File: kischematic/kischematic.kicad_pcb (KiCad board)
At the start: 2 copper layers, 26.7 x 50 mm, 109 parts, among them IC1 BlueNRG, IC10 128x64OLED, IC2 EFM32ZG108, IC3 BQ297xx, IC4 AAT3672IWO-4.2-1, IC5 TPS6223xx, IC6 APDS-9303, IC7 APDS-9303, IC8 BSD840NH6327XTSA1, IC9 MMA8653FC, J1 Screw_Terminal_1x02, J2 Screw_Terminal_1x01, J3 Screw_Terminal_1x01, J4 0, J5 Screw_Terminal_1x01, J6 Screw_Terminal_1x01, P1 CONN_01X01, P2 CONN_01X01, P3 CONN_01X01, P4 CONN_01X01, P5 CONN_01X01, P6 CONN_01X01, P7 CONN_01X01, P8 CONN_01X04, P9 CONN_01X04, SW1 SW_Push, SW2 SW_Push, U1 USB-C, U2 SWD_SPRING, Y1 32k, Y2 16M

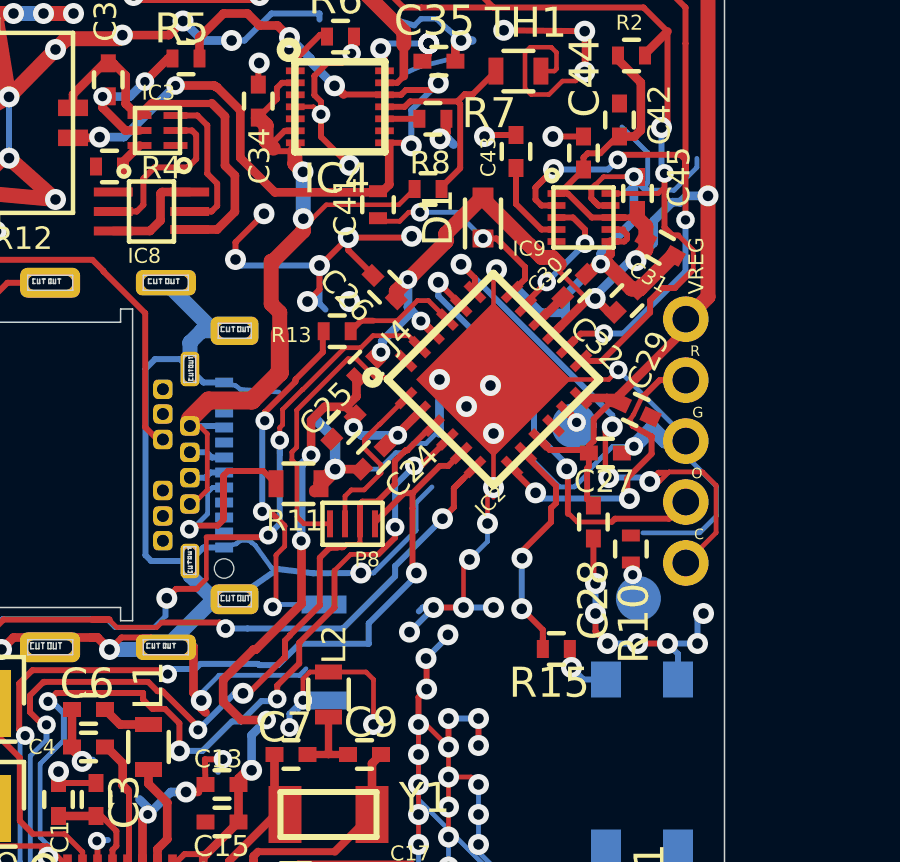
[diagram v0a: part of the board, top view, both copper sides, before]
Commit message: Routing problem caused by diode change; fix missing edge cuts.
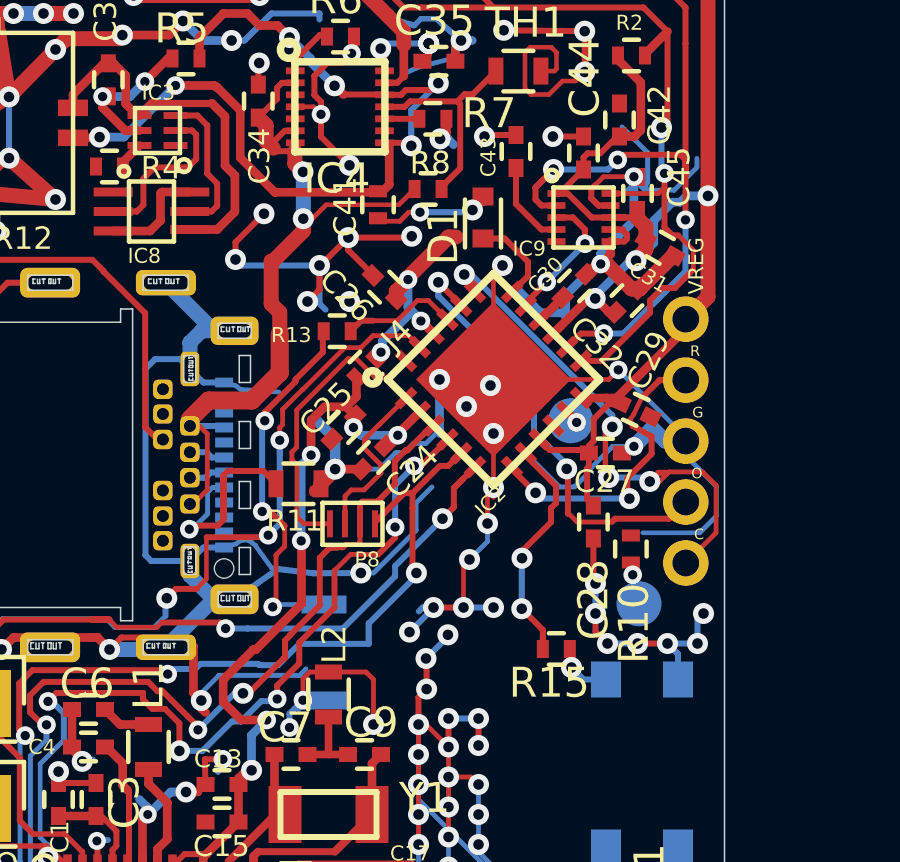
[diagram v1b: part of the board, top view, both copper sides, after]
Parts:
- C1, C2: value 100p -> HP100p
- C10, C8: value 15p -> HP15p
- C11, C13, C16, C4: value 1u -> HP1u
- C12, C14, C15, C5, C6: value 100n -> HP100n
- C17, C22: value 56p -> HP56p
- C18, C21, C23: value p5 -> HPp5
- C19, C20: value 1p3 -> HP1p3
- C3: value 150n -> HP150n
- C7, C9: value 22p -> HP22p
- D1: value D -> 0.8V FVD
- L1: value 10u -> DC-DC 4u7
- L4, L6: value 1n3 -> MQ 1n3
- L5: value 2n4 -> MQ 2n4
- L7: value 5n6 -> MQ 5n6
- L8: value 1u -> DC-DC 1u
- moved PIEZO 0.20 mm to (97.6, 47.4)
- moved PIEZOG 0.18 mm to (99.8, 53.5)
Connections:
- D1 pad 1: Net-(C41-Pad1) -> Net-(D1-Pad1)
- D1 pad 2: VREG -> Net-(C41-Pad1)
- IC2 pad 18: Net-(C41-Pad1) -> Net-(D1-Pad1)
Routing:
- net VREG: track 200.6 -> 193.8 mm
- net Net-(D1-Pad1): track 0.00 -> 3.05 mm
- net Net-(C41-Pad1): track 6.79 -> 4.03 mm
- net SWCLK: track 18.2 -> 17.5 mm
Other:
- outline, holes or cut-outs redrawn

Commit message: Mess.
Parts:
- removed PIEZO, PIEZOG: TEST, newlightmeter:SMALLWIREPAD
- added J7: 0, Resistors_SMD:R_0402, F.Cu at (95.5, 41.4)
- added TP1: TEST, newlightmeter:SMALLWIREPAD, B.Cu at (97.6, 47.4)
- added TP2: TEST, newlightmeter:SMALLWIREPAD, B.Cu at (99.9, 53.5)
- added U3: USB_PROTECTION, Housings_DFN_QFN:DFN-6-1EP_2x2mm_Pitch0.5mm, F.Cu at (81.2, 46.6)
- moved D1 1.00 mm to (94.7, 39.6)
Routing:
- net VREG: track 193.8 -> 198.4 mm, vias 21 -> 22
- net GND: track 476.7 -> 472.4 mm
- net (no net): track 2.40 -> 5.41 mm
- net Net-(C41-Pad1): track 4.03 -> 4.46 mm, vias 2 -> 0
- net ACCELINT1: track 4.48 -> 4.52 mm, vias 2 -> 0

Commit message: More work on USB stuff.
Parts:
- U3: value USB_PROTECTION -> FT220X; footprint Housings_DFN_QFN:DFN-6-1EP_2x2mm_Pitch0.5mm -> newlightmeter:QFN_16
- moved U3 11.0 mm to (71.7, 52.1)
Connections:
- U1 pad B6: Net-(U1-PadA7) -> Net-(U1-PadA6)
- U1 pad B7: Net-(U1-PadA6) -> Net-(U1-PadA7)
- U3 pad 1: Net-(U1-PadA6) -> Net-(U3-Pad1)
- U3 pad 2: Net-(U1-PadA7) -> Net-(U3-Pad2)
- U3 pad 4: (no net) -> Net-(U3-Pad4)
- U3 pad 5: (no net) -> Net-(U3-Pad5)
- U3 pad 6: VUSB -> Net-(U3-Pad6)
- U3 pad 7: GND -> Net-(U3-Pad7)
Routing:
- net Net-(U1-PadA7): track 1.27 -> 0.05 mm
- net Net-(U1-PadA6): track 1.26 -> 0.06 mm
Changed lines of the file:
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@@
 (kicad_pcb (version 20160815) (host pcbnew "(2016-12-18 revision 3ffa37c)-master")
   (general
-    (links 266)
-    (no_connects 13)
+    (links 261)
+    (no_connects 10)
     (area 75.974999 24.974999 102.725001 75.025001)
     (thickness 1.6)
     (drawings 272)
-    (tracks 2039)
+    (tracks 2033)
     (zones 0)
     (modules 111)
-    (nets 109)
+    (nets 125)
   )
   (page A4)
@@
   (net 107 "Net-(D1-Pad1)")
   (net 108 "Net-(U3-Pad3)")
+  (net 109 "Net-(U3-Pad7)")
+  (net 110 "Net-(U3-Pad6)")
+  (net 111 "Net-(U3-Pad5)")
+  (net 112 "Net-(U3-Pad4)")
+  (net 113 "Net-(U3-Pad2)")
+  (net 114 "Net-(U3-Pad1)")
+  (net 115 "Net-(U3-Pad8)")
+  (net 116 "Net-(U3-Pad9)")
+  (net 117 "Net-(U3-Pad10)")
+  (net 118 "Net-(U3-Pad11)")
+  (net 119 "Net-(U3-Pad12)")
+  (net 120 "Net-(U3-Pad13)")
+  (net 121 "Net-(U3-Pad14)")
+  (net 122 "Net-(U3-Pad15)")
+  (net 123 "Net-(U3-Pad16)")
+  (net 124 "Net-(U3-Pad17)")
   (net_class Default "This is the default net class."
     (clearance 0.1525)
@@
     (add_net "Net-(U1-PadB3)")
     (add_net "Net-(U1-PadB8)")
+    (add_net "Net-(U3-Pad1)")
+    (add_net "Net-(U3-Pad10)")
+    (add_net "Net-(U3-Pad11)")
+    (add_net "Net-(U3-Pad12)")
+    (add_net "Net-(U3-Pad13)")
+    (add_net "Net-(U3-Pad14)")
+    (add_net "Net-(U3-Pad15)")
+    (add_net "Net-(U3-Pad16)")
+    (add_net "Net-(U3-Pad17)")
+    (add_net "Net-(U3-Pad2)")
     (add_net "Net-(U3-Pad3)")
+    (add_net "Net-(U3-Pad4)")
+    (add_net "Net-(U3-Pad5)")
+    (add_net "Net-(U3-Pad6)")
+    (add_net "Net-(U3-Pad7)")
+    (add_net "Net-(U3-Pad8)")
+    (add_net "Net-(U3-Pad9)")
     (add_net PIEZO)
     (add_net PIEZOGND)
@@
     (add_net VUSB)
   )
-  (module Housings_DFN_QFN:DFN-6-1EP_2x2mm_Pitch0.5mm (layer F.Cu)
-    (at 81.2 46.62)
-    (descr "DC6 Package; 6-Lead Plastic DFN (2mm x 2mm) (see Linear Technology DFN_6_05-08-1703.pdf)")
-    (tags "DFN 0.5")
-    (attr smd)
-    (fp_text reference U3 (at 0 -2.05) (layer F.SilkS)
-      (effects (font (size 1 1) (thickness 0.15)))
-    )
-    (fp_text value USB_PROTECTION (at 0 2.05) (layer F.Fab)
-      (effects (font (size 1 1) (thickness 0.15)))
-    )
-    (fp_line (start -1.35 -1.125) (end 0.575 -1.125) (layer F.SilkS) (width 0.15))
-    (fp_line (start -0.575 1.125) (end 0.575 1.125) (layer F.SilkS) (width 0.15))
-    (fp_line (start -1.55 1.3) (end 1.55 1.3) (layer F.CrtYd) (width 0.05))
-    (fp_line (start -1.55 -1.3) (end 1.55 -1.3) (layer F.CrtYd) (width 0.05))
-    (fp_line (start 1.55 -1.3) (end 1.55 1.3) (layer F.CrtYd) (width 0.05))
-    (fp_line (start -1.55 -1.3) (end -1.55 1.3) (layer F.CrtYd) (width 0.05))
-    (fp_line (start -1 0) (end 0 -1) (layer F.Fab) (width 0.15))
-    (fp_line (start -1 1) (end -1 0) (layer F.Fab) (width 0.15))
-    (fp_line (start 1 1) (end -1 1) (layer F.Fab) (width 0.15))
-    (fp_line (start 1 -1) (end 1 1) (layer F.Fab) (width 0.15))
-    (fp_line (start 0 -1) (end 1 -1) (layer F.Fab) (width 0.15))
-    (pad 7 smd rect (at 0 -0.355) (size 0.61 0.71) (layers F.Cu F.Paste F.Mask)
-      (net 1 GND) (solder_paste_margin_ratio -0.2))
-    (pad 7 smd rect (at 0 0.355) (size 0.61 0.71) (layers F.Cu F.Paste F.Mask)
-      (net 1 GND) (solder_paste_margin_ratio -0.2))
-    (pad 6 smd rect (at 0.925 -0.5) (size 0.7 0.25) (layers F.Cu F.Paste F.Mask)
-      (net 43 VUSB))
-    (pad 5 smd rect (at 0.925 0) (size 0.7 0.25) (layers F.Cu F.Paste F.Mask))
-    (pad 4 smd rect (at 0.925 0.5) (size 0.7 0.25) (layers F.Cu F.Paste F.Mask))
-    (pad 3 smd rect (at -0.925 0.5) (size 0.7 0.25) (layers F.Cu F.Paste F.Mask)
-      (net 108 "Net-(U3-Pad3)"))
-    (pad 2 smd rect (at -0.925 0) (size 0.7 0.25) (layers F.Cu F.Paste F.Mask)
-      (net 57 "Net-(U1-PadA7)"))
-    (pad 1 smd rect (at -0.925 -0.5) (size 0.7 0.25) (layers F.Cu F.Paste F.Mask)
-      (net 56 "Net-(U1-PadA6)"))
-    (model Housings_DFN_QFN.3dshapes/DFN-6-1EP_2x2mm_Pitch0.5mm.wrl
-      (at (xyz 0 0 0))
-      (scale (xyz 1 1 1))
-      (rotate (xyz 0 0 0))
+  (module newlightmeter:QFN_16 (layer F.Cu)
+    (at 71.7 52.125)
+    (attr smd)
+    (fp_text reference U3 (at 0 -3.55) (layer F.SilkS)
+      (effects (font (size 1 1) (thickness 0.15)))
+    )
+    (fp_text value FT220X (at 0 3.55) (layer F.Fab)
+      (effects (font (size 1 1) (thickness 0.15)))
     )
+    (fp_line (start -2 -1.625) (end -1.625 -2) (layer F.SilkS) (width 0.15))
+    (fp_line (start 1.625 -2) (end 2 -2) (layer F.SilkS) (width 0.15))
+    (fp_line (start 2 -2) (end 2 -1.625) (layer F.SilkS) (width 0.15))
+    (fp_line (start -1.625 2) (end -2 2) (layer F.SilkS) (width 0.15))
+    (fp_line (start -2 2) (end -2 1.625) (layer F.SilkS) (width 0.15))
+    (fp_line (start 1.625 2) (end 2 2) (layer F.SilkS) (width 0.15))
+    (fp_line (start 2 2) (end 2 1.625) (layer F.SilkS) (width 0.15))
+    (fp_line (start -2.3 -2.3) (end 2.3 -2.3) (layer F.CrtYd) (width 0.05))
+    (fp_line (start 2.3 -2.3) (end 2.3 2.3) (layer F.CrtYd) (width 0.05))
+    (fp_line (start 2.3 2.3) (end -2.3 2.3) (layer F.CrtYd) (width 0.05))
+    (fp_line (start -2.3 2.3) (end -2.3 -2.3) (layer F.CrtYd) (width 0.05))
+    (pad 1 smd rect (at -2 -0.975 90) (size 0.4 1.1) (layers F.Cu F.Paste F.Mask)
+      (net 114 "Net-(U3-Pad1)"))
+    (pad 2 smd rect (at -2 -0.325 90) (size 0.4 1.1) (layers F.Cu F.Paste F.Mask)
+      (net 113 "Net-(U3-Pad2)"))
+    (pad 3 smd rect (at -2 0.325 90) (size 0.4 1.1) (layers F.Cu F.Paste F.Mask)
+      (net 108 "Net-(U3-Pad3)"))
+    (pad 4 smd rect (at -2 0.975 90) (size 0.4 1.1) (layers F.Cu F.Paste F.Mask)
+      (net 112 "Net-(U3-Pad4)"))
+    (pad 5 smd rect (at -0.975 2) (size 0.4 1.1) (layers F.Cu F.Paste F.Mask)
+      (net 111 "Net-(U3-Pad5)"))
+    (pad 6 smd rect (at -0.325 2) (size 0.4 1.1) (layers F.Cu F.Paste F.Mask)
+      (net 110 "Net-(U3-Pad6)"))
+    (pad 7 smd rect (at 0.325 2) (size 0.4 1.1) (layers F.Cu F.Paste F.Mask)
+      (net 109 "Net-(U3-Pad7)"))
+    (pad 8 smd rect (at 0.975 2) (size 0.4 1.1) (layers F.Cu F.Paste F.Mask)
+      (net 115 "Net-(U3-Pad8)"))
+    (pad 9 smd rect (at 2 0.975 90) (size 0.4 1.1) (layers F.Cu F.Paste F.Mask)
+      (net 116 "Net-(U3-Pad9)"))
+    (pad 10 smd rect (at 2 0.325 90) (size 0.4 1.1) (layers F.Cu F.Paste F.Mask)
+      (net 117 "Net-(U3-Pad10)"))
+    (pad 11 smd rect (at 2 -0.325 90) (size 0.4 1.1) (layers F.Cu F.Paste F.Mask)
+      (net 118 "Net-(U3-Pad11)"))
+    (pad 12 smd rect (at 2 -0.975 90) (size 0.4 1.1) (layers F.Cu F.Paste F.Mask)
+      (net 119 "Net-(U3-Pad12)"))
+    (pad 13 smd rect (at 0.975 -2) (size 0.4 1.1) (layers F.Cu F.Paste F.Mask)
+      (net 120 "Net-(U3-Pad13)"))
+    (pad 14 smd rect (at 0.325 -2) (size 0.4 1.1) (layers F.Cu F.Paste F.Mask)
+      (net 121 "Net-(U3-Pad14)"))
+    (pad 15 smd rect (at -0.325 -2) (size 0.4 1.1) (layers F.Cu F.Paste F.Mask)
+      (net 122 "Net-(U3-Pad15)"))
+    (pad 16 smd rect (at -0.975 -2) (size 0.4 1.1) (layers F.Cu F.Paste F.Mask)
+      (net 123 "Net-(U3-Pad16)"))
+    (pad 17 smd rect (at 0 -0.075) (size 2.15 2.15) (layers F.Cu F.Paste F.Mask)
+      (net 124 "Net-(U3-Pad17)"))
   )
   (module newlightmeter:AN2051 (layer F.Cu)
@@
       (net 43 VUSB))
     (pad B6 thru_hole roundrect (at 0.425 -1.14 90) (size 0.65 0.65) (drill 0.4) (layers *.Cu *.Mask)(roundrect_rratio 0.25)
-      (net 57 "Net-(U1-PadA7)"))
+      (net 56 "Net-(U1-PadA6)"))
     (pad B11 thru_hole roundrect (at -2.525 -2.04 90) (size 0.65 0.65) (drill 0.4) (layers *.Cu *.Mask)(roundrect_rratio 0.25)
       (net 65 "Net-(U1-PadB11)"))
@@
       (net 66 "Net-(R12-Pad2)"))
     (pad B7 thru_hole roundrect (at -0.425 -1.14 90) (size 0.65 0.65) (drill 0.4) (layers *.Cu *.Mask)(roundrect_rratio 0.25)
-      (net 56 "Net-(U1-PadA6)"))
+      (net 57 "Net-(U1-PadA7)"))
     (pad S4 thru_hole roundrect (at 6.075 -5.8 90) (size 1 2) (drill oval 0.5 1.5) (layers *.Cu *.Mask)(roundrect_rratio 0.25)
       (net 1 GND))
@@
   (segment (start 101.24 28.9) (end 100.73 29.41) (width 0.16) (layer F.Cu) (net 53) (status 10))
   (segment (start 101.31 28.9) (end 101.24 28.9) (width 0.16) (layer F.Cu) (net 53) (status 30))
-  (segment (start 85.395 49.275) (end 85.57 49.1) (width 0.2) (layer B.Cu) (net 56))
-  (segment (start 85.57 49.1) (end 86.02 49.1) (width 0.2) (layer B.Cu) (net 56) (status 20))
-  (segment (start 84.88 49.275) (end 85.395 49.275) (width 0.2) (layer B.Cu) (net 56) (status 10))
-  (segment (start 84.88 49.275) (end 84.835 49.275) (width 0.16) (layer B.Cu) (net 56) (status 30))
-  (segment (start 85.435 48.425) (end 85.61 48.6) (width 0.2) (layer B.Cu) (net 57))
-  (segment (start 85.61 48.6) (end 86.02 48.6) (width 0.2) (layer B.Cu) (net 57) (status 20))
-  (segment (start 84.88 48.425) (end 85.435 48.425) (width 0.2) (layer B.Cu) (net 57) (status 10))
-  (segment (start 84.88 48.425) (end 84.935 48.425) (width 0.16) (layer B.Cu) (net 57) (status 30))
+  (segment (start 84.88 48.425) (end 84.935 48.425) (width 0.16) (layer B.Cu) (net 56) (status 30))
+  (segment (start 84.88 49.275) (end 84.835 49.275) (width 0.16) (layer B.Cu) (net 57) (status 30))
   (segment (start 83.98 48) (end 83.8 48) (width 0.2) (layer F.Cu) (net 66))
   (segment (start 83.8 48) (end 83.39 47.59) (width 0.2) (layer F.Cu) (net 66))

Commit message: Remove unnecessary (I hope) D+/- connection.
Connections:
- U1 pad B6: Net-(U1-PadA6) -> Net-(U1-PadB6)
- U1 pad B7: Net-(U1-PadA7) -> Net-(U1-PadB7)
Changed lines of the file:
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@@
 (kicad_pcb (version 20160815) (host pcbnew "(2016-12-18 revision 3ffa37c)-master")
   (general
-    (links 261)
-    (no_connects 10)
+    (links 259)
+    (no_connects 8)
     (area 75.974999 24.974999 102.725001 75.025001)
     (thickness 1.6)
@@
     (zones 0)
     (modules 111)
-    (nets 125)
+    (nets 127)
   )
   (page A4)
@@
   (net 123 "Net-(U3-Pad16)")
   (net 124 "Net-(U3-Pad17)")
+  (net 125 "Net-(U1-PadB6)")
+  (net 126 "Net-(U1-PadB7)")
   (net_class Default "This is the default net class."
     (clearance 0.1525)
@@
     (add_net "Net-(U1-PadB2)")
     (add_net "Net-(U1-PadB3)")
+    (add_net "Net-(U1-PadB6)")
+    (add_net "Net-(U1-PadB7)")
     (add_net "Net-(U1-PadB8)")
     (add_net "Net-(U3-Pad1)")
@@
       (net 43 VUSB))
     (pad B6 thru_hole roundrect (at 0.425 -1.14 90) (size 0.65 0.65) (drill 0.4) (layers *.Cu *.Mask)(roundrect_rratio 0.25)
-      (net 56 "Net-(U1-PadA6)"))
+      (net 125 "Net-(U1-PadB6)"))
     (pad B11 thru_hole roundrect (at -2.525 -2.04 90) (size 0.65 0.65) (drill 0.4) (layers *.Cu *.Mask)(roundrect_rratio 0.25)
       (net 65 "Net-(U1-PadB11)"))
@@
       (net 66 "Net-(R12-Pad2)"))
     (pad B7 thru_hole roundrect (at -0.425 -1.14 90) (size 0.65 0.65) (drill 0.4) (layers *.Cu *.Mask)(roundrect_rratio 0.25)
-      (net 57 "Net-(U1-PadA7)"))
+      (net 126 "Net-(U1-PadB7)"))
     (pad S4 thru_hole roundrect (at 6.075 -5.8 90) (size 1 2) (drill oval 0.5 1.5) (layers *.Cu *.Mask)(roundrect_rratio 0.25)
       (net 1 GND))
@@
   (segment (start 101.24 28.9) (end 100.73 29.41) (width 0.16) (layer F.Cu) (net 53) (status 10))
   (segment (start 101.31 28.9) (end 101.24 28.9) (width 0.16) (layer F.Cu) (net 53) (status 30))
-  (segment (start 84.88 48.425) (end 84.935 48.425) (width 0.16) (layer B.Cu) (net 56) (status 30))
-  (segment (start 84.88 49.275) (end 84.835 49.275) (width 0.16) (layer B.Cu) (net 57) (status 30))
   (segment (start 83.98 48) (end 83.8 48) (width 0.2) (layer F.Cu) (net 66))
   (segment (start 83.8 48) (end 83.39 47.59) (width 0.2) (layer F.Cu) (net 66))
@@
   (segment (start 95.675 41.6) (end 95.3 40.95) (width 0.16) (layer F.Cu) (net 107))
   (segment (start 95.75 41.7) (end 95.675 41.6) (width 0.16) (layer F.Cu) (net 107))
+  (segment (start 84.88 48.425) (end 84.935 48.425) (width 0.16) (layer B.Cu) (net 125) (status 30))
+  (segment (start 84.88 49.275) (end 84.835 49.275) (width 0.16) (layer B.Cu) (net 126) (status 30))
   (zone (net 1) (net_name GND) (layer F.Cu) (hatch edge 0.508)
     (connect_pads (clearance 0.18))
